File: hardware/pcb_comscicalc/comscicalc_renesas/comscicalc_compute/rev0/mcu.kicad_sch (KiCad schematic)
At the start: 30 parts, among them IC1 R7FA4M3AF3CFM#AA0, J1 Conn_02x14_Odd_Even, J2 Conn_02x14_Odd_Even, SW1 SSSS211603, Y1 FL2400022

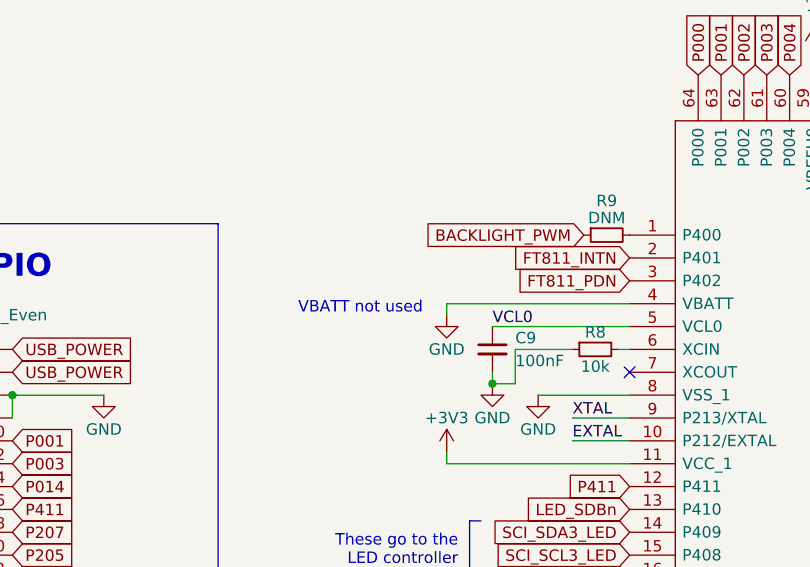
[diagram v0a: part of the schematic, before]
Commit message: rev0 of hardware works fine with VBATT pin left open. Starting rev1 using rp2040
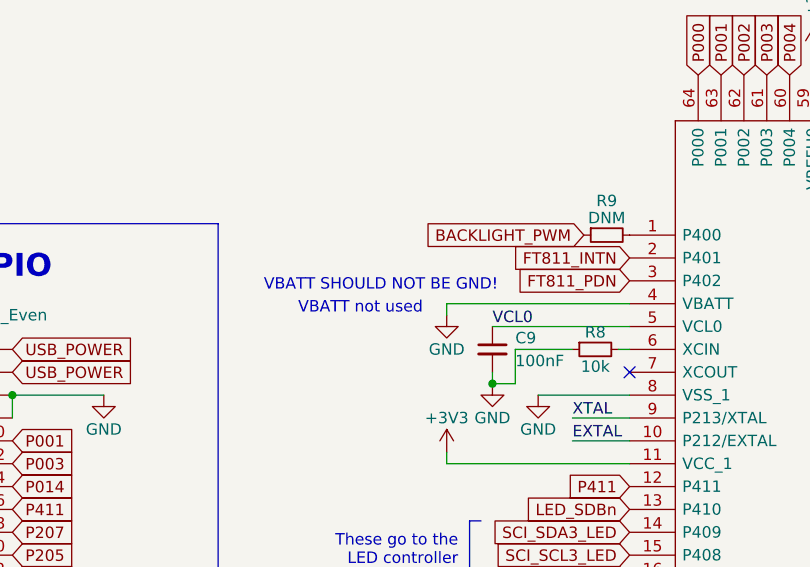
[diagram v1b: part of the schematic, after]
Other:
- note added: "VBATT SHOULD NOT BE GND!"
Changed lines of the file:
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@@
     (effects (font (size 2.54 2.54) (thickness 0.508) bold) (justify left bottom))
+  )
+  (text "VBATT SHOULD NOT BE GND!" (at 138.43 63.5 0)
+    (effects (font (size 1.27 1.27)) (justify left bottom))
   )
   (text "These go to the\nLED controller" (at 160.02 93.98 180)
